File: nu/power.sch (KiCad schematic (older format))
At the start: 0 parts

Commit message: Added block diagram, and added some components to the schematic that will end up being removed :/
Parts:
- added D? (x3): TL431ACDBZR, Package_TO_SOT_SMD:SOT-23, symbol custom:TL431ACDBZR
- added J?: S4B-XH-A, Connector_PinHeader_2.54mm:PinHeader_1x04_P2.54mm_Horizontal, symbol custom:S4B-XH-A
- added Q? (x3): FZT705, Package_TO_SOT_SMD:SOT-223, symbol custom:FZT705
- added R? (x3): RCL12254R30JNEG, symbol custom:RCL12254R30JNEG
- added R? (x3): RC0603JR-070RL, Resistor_SMD:R_0603_1608Metric, symbol custom:RC0603JR-070RL
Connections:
- net labels added: GND
- wire segments 0 -> 57
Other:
- note added: "BATTERY\nTAPS"
- note added: "TRIGGER AT 2.4 V"

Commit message: Updated block diagram
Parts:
- removed D? (x3): TL431ACDBZR, Package_TO_SOT_SMD:SOT-23, symbol custom:TL431ACDBZR
- removed Q? (x3): FZT705, Package_TO_SOT_SMD:SOT-223, symbol custom:FZT705
- removed R? (x3): RCL12254R30JNEG, symbol custom:RCL12254R30JNEG
- removed R? (x3): RC0603JR-070RL, Resistor_SMD:R_0603_1608Metric, symbol custom:RC0603JR-070RL
- added J? (x2): S4B-XH-A, Connector_PinHeader_2.54mm:PinHeader_1x04_P2.54mm_Horizontal, symbol nu-rescue:S4B-XH-A-custom
- J?: symbol custom:S4B-XH-A -> nu-rescue:S4B-XH-A-custom
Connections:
- net labels removed: GND
- wire segments 57 -> 24
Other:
- note removed: "TRIGGER AT 2.4 V"

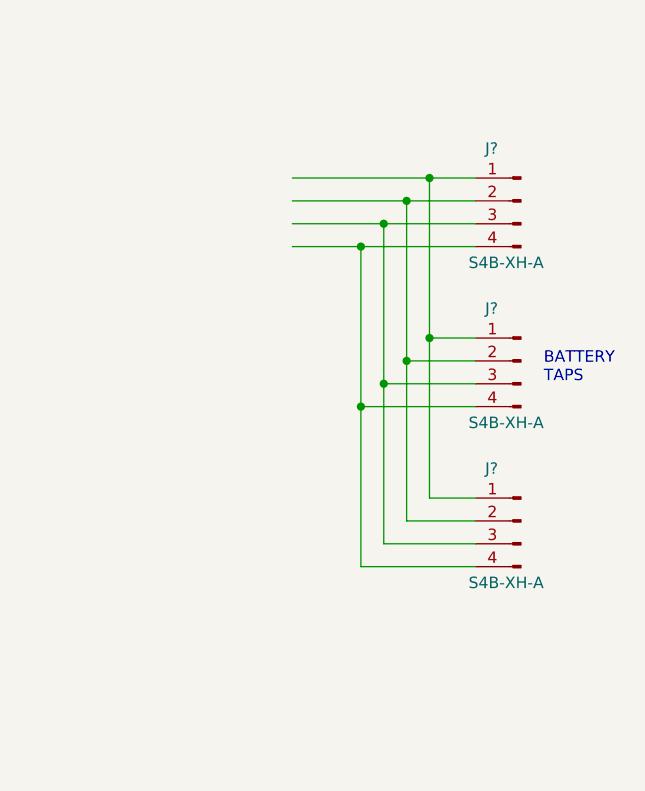
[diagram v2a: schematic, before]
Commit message: added microcontroller sheet
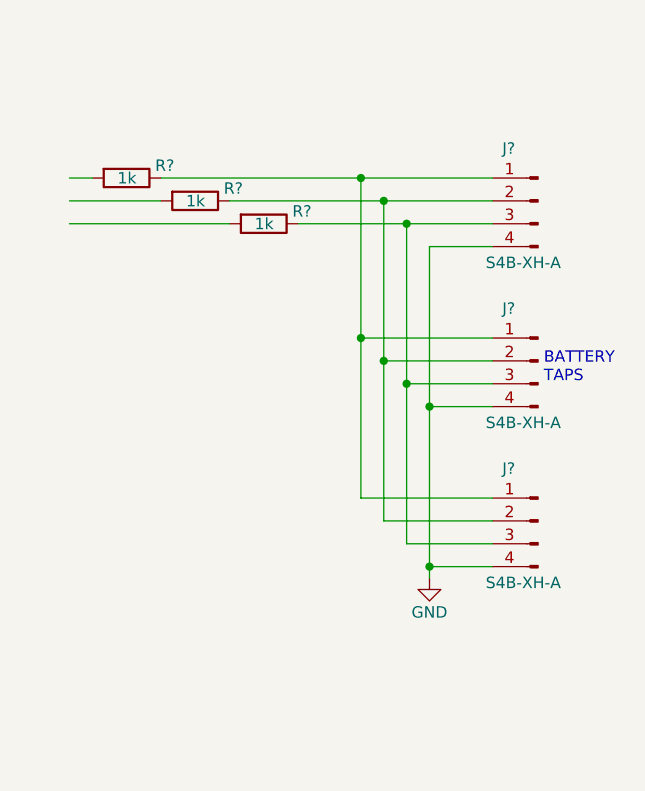
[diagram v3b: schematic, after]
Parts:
- added R? (x3): RC0603JR-071KL, 0603, symbol custom:RC0603JR-071KL
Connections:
- net labels added: GND
- wire segments 24 -> 27
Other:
- moved on the sheet: J?
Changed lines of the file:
@@
 $Descr A4 11693 8268
 encoding utf-8
-Sheet 2 3
+Sheet 2 4
 Title ""
 Date ""
@@
 L nu-rescue:S4B-XH-A-custom J?
 U 1 1 5C34712D
-P 5950 3000
+P 6025 3000
 AR Path="/5C34712D" Ref="J?"  Part="1"
 AR Path="/5C100B31/5C34712D" Ref="J?"  Part="1"
-F 0 "J?" H 6050 3200 50  0000 L BNN
-F 1 "S4B-XH-A" H 5850 2700 50  0000 L BNN
-F 2 "Connector_PinHeader_2.54mm:PinHeader_1x04_P2.54mm_Horizontal" H 5950 2600 50  0001 L BNN
-F 3 "eXH.pdf" H 5950 2500 50  0001 L BNN
-	1    5950 3000
+F 0 "J?" H 6125 3200 50  0000 L BNN
+F 1 "S4B-XH-A" H 5925 2700 50  0000 L BNN
+F 2 "Connector_PinHeader_2.54mm:PinHeader_1x04_P2.54mm_Horizontal" H 6025 2600 50  0001 L BNN
+F 3 "eXH.pdf" H 6025 2500 50  0001 L BNN
+	1    6025 3000
 	-1   0    0    -1
 $EndComp
@@
 L nu-rescue:S4B-XH-A-custom J?
 U 1 1 5C36BCF1
-P 5950 3700
+P 6025 3700
 AR Path="/5C36BCF1" Ref="J?"  Part="1"
 AR Path="/5C100B31/5C36BCF1" Ref="J?"  Part="1"
-F 0 "J?" H 6050 3900 50  0000 L BNN
-F 1 "S4B-XH-A" H 5850 3400 50  0000 L BNN
-F 2 "Connector_PinHeader_2.54mm:PinHeader_1x04_P2.54mm_Horizontal" H 5950 3300 50  0001 L BNN
-F 3 "eXH.pdf" H 5950 3200 50  0001 L BNN
-	1    5950 3700
+F 0 "J?" H 6125 3900 50  0000 L BNN
+F 1 "S4B-XH-A" H 5925 3400 50  0000 L BNN
+F 2 "Connector_PinHeader_2.54mm:PinHeader_1x04_P2.54mm_Horizontal" H 6025 3300 50  0001 L BNN
+F 3 "eXH.pdf" H 6025 3200 50  0001 L BNN
+	1    6025 3700
 	-1   0    0    -1
 $EndComp
@@
 L nu-rescue:S4B-XH-A-custom J?
 U 1 1 5C36BD2D
-P 5950 2300
+P 6025 2300
 AR Path="/5C36BD2D" Ref="J?"  Part="1"
 AR Path="/5C100B31/5C36BD2D" Ref="J?"  Part="1"
-F 0 "J?" H 6050 2500 50  0000 L BNN
-F 1 "S4B-XH-A" H 5850 2000 50  0000 L BNN
-F 2 "Connector_PinHeader_2.54mm:PinHeader_1x04_P2.54mm_Horizontal" H 5950 1900 50  0001 L BNN
-F 3 "eXH.pdf" H 5950 1800 50  0001 L BNN
-	1    5950 2300
+F 0 "J?" H 6125 2500 50  0000 L BNN
+F 1 "S4B-XH-A" H 5925 2000 50  0000 L BNN
+F 2 "Connector_PinHeader_2.54mm:PinHeader_1x04_P2.54mm_Horizontal" H 6025 1900 50  0001 L BNN
+F 3 "eXH.pdf" H 6025 1800 50  0001 L BNN
+	1    6025 2300
 	-1   0    0    -1
 $EndComp
 Wire Wire Line
-	5750 3600 5550 3600
+	5825 3600 5250 3600
 Wire Wire Line
-	5550 3600 5550 2900
+	5250 3600 5250 2900
 Wire Wire Line
-	5550 2200 5750 2200
+	5250 2200 5825 2200
+Connection ~ 5250 2200
 Wire Wire Line
-	5550 2200 4950 2200
-Connection ~ 5550 2200
+	5825 2300 5350 2300
 Wire Wire Line
-	5750 2300 5450 2300
+	5825 2400 5450 2400
 Wire Wire Line
-	5750 2400 5350 2400
+	5825 2500 5550 2500
 Wire Wire Line
-	5750 2500 5250 2500
+	5825 2900 5250 2900
 Wire Wire Line
-	5750 2900 5550 2900
-Connection ~ 5550 2900
+	5250 2900 5250 2200
 Wire Wire Line
-	5550 2900 5550 2200
+	5825 3700 5350 3700
 Wire Wire Line
-	5750 3700 5450 3700
+	5350 3700 5350 3000
+Connection ~ 5350 2300
 Wire Wire Line
-	5450 3700 5450 3000
-Connection ~ 5450 2300
+	5825 3800 5450 3800
 Wire Wire Line
-	5450 2300 4950 2300
+	5450 3800 5450 3100
+Connection ~ 5450 2400
 Wire Wire Line
-	5750 3800 5350 3800
+	5825 3900 5550 3900
 Wire Wire Line
-	5350 3800 5350 3100
-Connection ~ 5350 2400
+	5550 3900 5550 3200
 Wire Wire Line
-	5350 2400 4950 2400
+	5825 3000 5350 3000
 Wire Wire Line
-	5750 3900 5250 3900
+	5350 3000 5350 2300
 Wire Wire Line
-	5250 3900 5250 3200
-Connection ~ 5250 2500
+	5825 3100 5450 3100
 Wire Wire Line
-	5250 2500 4950 2500
+	5450 3100 5450 2400
 Wire Wire Line
-	5750 3000 5450 3000
-Connection ~ 5450 3000
+	5825 3200 5550 3200
 Wire Wire Line
-	5450 3000 5450 2300
+	5550 3200 5550 2500
+$Comp
+L power:GND #PWR?
+U 1 1 5C3D714A
+P 5550 3950
+F 0 "#PWR?" H 5550 3700 50  0001 C CNN
+F 1 "GND" H 5550 3800 50  0000 C CNN
+F 2 "" H 5550 3950 50  0001 C CNN
+F 3 "" H 5550 3950 50  0001 C CNN
+	1    5550 3950
+	1    0    0    -1
+$EndComp
 Wire Wire Line
-	5750 3100 5350 3100
-Connection ~ 5350 3100
+	5550 3950 5550 3900
+$Comp
+L custom:RC0603JR-071KL R?
+U 1 1 5C3DB61F
+P 4225 2200
+F 0 "R?" V 4200 2325 50  0000 L BNN
+F 1 "RC0603JR-071KL" V 4350 1875 50  0001 L BNN
+F 2 "0603" V 4425 2100 50  0001 L BNN
+F 3 "RC0603JR-071KL.pdf" V 4165 2160 50  0001 C CNN
+F 4 "1k" V 4255 2160 50  0000 L BNN "Resistance"
+	1    4225 2200
+	0    1    1    0
+$EndComp
+$Comp
+L custom:RC0603JR-071KL R?
+U 1 1 5C3DB6C2
+P 4525 2300
+F 0 "R?" V 4500 2425 50  0000 L BNN
+F 1 "RC0603JR-071KL" V 4650 1975 50  0001 L BNN
+F 2 "0603" V 4725 2200 50  0001 L BNN
+F 3 "RC0603JR-071KL.pdf" V 4465 2260 50  0001 C CNN
+F 4 "1k" V 4555 2260 50  0000 L BNN "Resistance"
+	1    4525 2300
+	0    1    1    0
+$EndComp
+$Comp
+L custom:RC0603JR-071KL R?
+U 1 1 5C3DBA77
+P 4825 2400
+F 0 "R?" V 4800 2525 50  0000 L BNN
+F 1 "RC0603JR-071KL" V 4950 2075 50  0001 L BNN
+F 2 "0603" V 5025 2300 50  0001 L BNN
+F 3 "RC0603JR-071KL.pdf" V 4765 2360 50  0001 C CNN
+F 4 "1k" V 4855 2360 50  0000 L BNN "Resistance"
+	1    4825 2400
+	0    1    1    0
+$EndComp
 Wire Wire Line
-	5350 3100 5350 2400
+	4975 2400 5450 2400
 Wire Wire Line
-	5750 3200 5250 3200
-Connection ~ 5250 3200
+	4675 2300 5350 2300
 Wire Wire Line
-	5250 3200 5250 2500
+	4375 2200 5250 2200
+Wire Wire Line
+	4675 2400 3975 2400
+Wire Wire Line
+	4375 2300 3975 2300
+Wire Wire Line
+	4075 2200 3975 2200
+Connection ~ 5550 3900
+Connection ~ 5550 3200
+Connection ~ 5450 3100
+Connection ~ 5350 3000
+Connection ~ 5250 2900
 $EndSCHEMATC
